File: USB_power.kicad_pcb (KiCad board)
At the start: 2 copper layers, 42.5 x 65.5 mm, 30 parts, among them J1 PWR_IN, J2 USB_A_Stacked, J3 Power_check, J4 USB_C_Receptacle_USB2.0_16P, J5 USB_A_Stacked

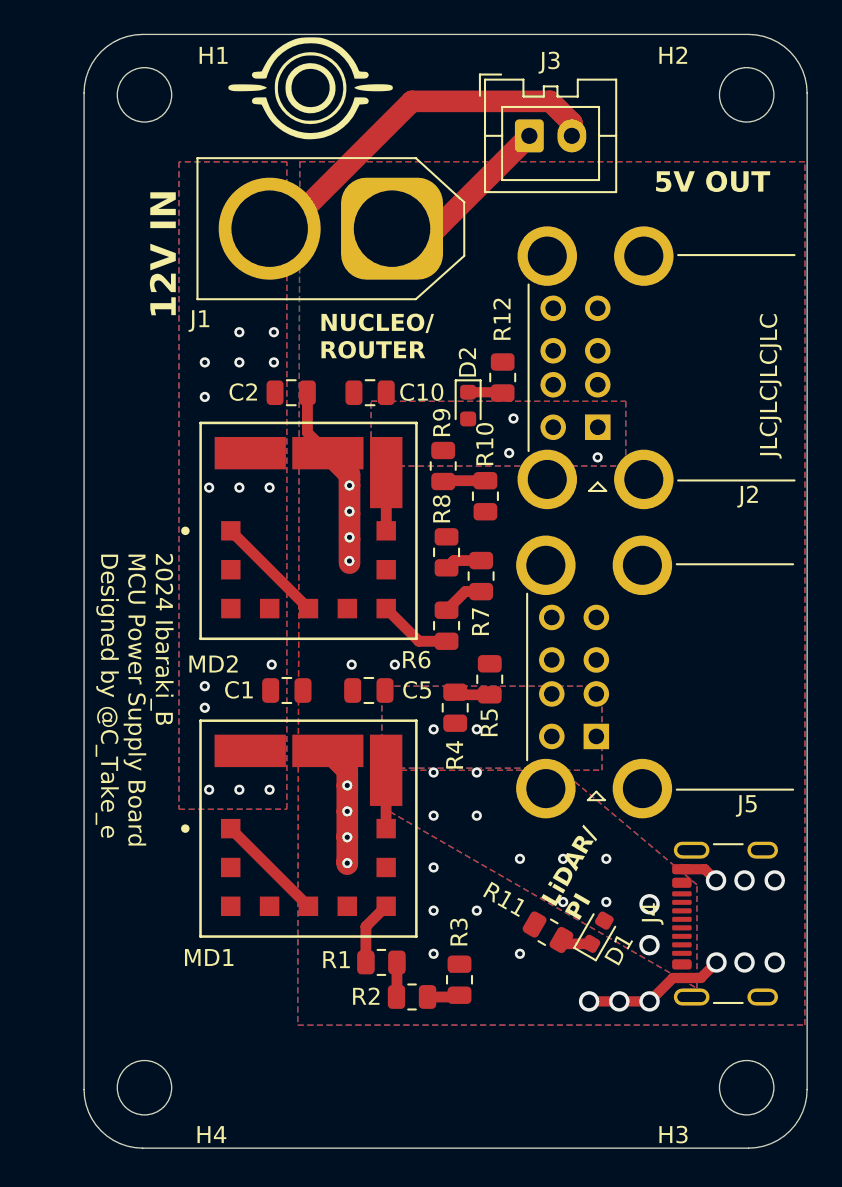
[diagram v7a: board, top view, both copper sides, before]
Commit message: ヒューズ追加、外形削除
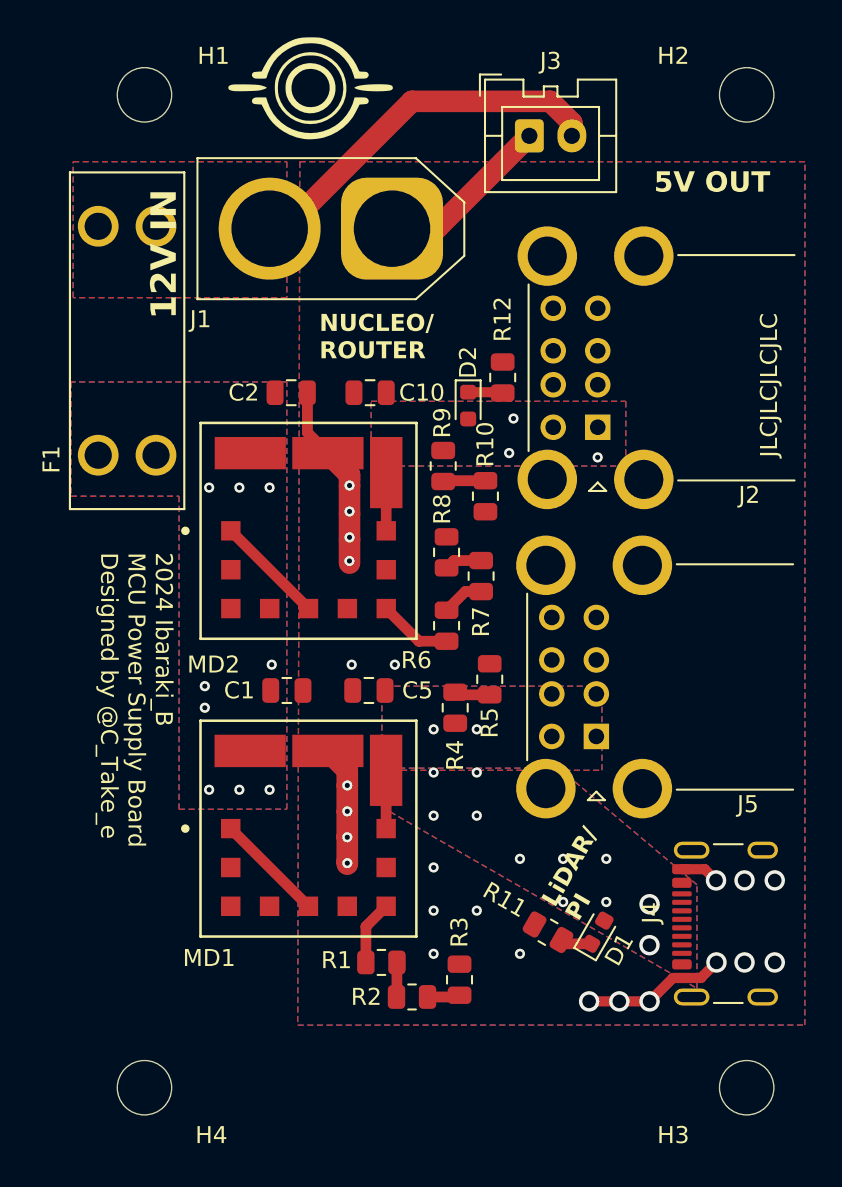
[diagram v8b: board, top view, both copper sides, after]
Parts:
- added F1: Fuse, FUSE_3557:FUSE_3557-2, F.Cu at (130.3, 89.9)
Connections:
- C1 pad 1: +BATT -> Battery
- C2 pad 1: +BATT -> Battery
- MD1 pad 2: +BATT -> Battery
- MD2 pad 2: +BATT -> Battery
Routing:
- net Battery: vias 0 -> 9
- net +BATT: vias 15 -> 0
- added copper zone on B.Cu, net Battery
- added copper zone on F.Cu, net Battery
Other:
- board outline removed
